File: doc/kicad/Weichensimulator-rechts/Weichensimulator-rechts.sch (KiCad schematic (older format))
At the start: 9 parts, among them J1 Conn_01x02_Male, J2 Power, J3 Conn_01x02_Male, K1 HFD2_005-S-L2-D

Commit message: v2.0 hinzugefügt
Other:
- moved on the sheet: H1
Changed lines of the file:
@@
 Wire Wire Line
 	5450 3250 5450 3150
-Connection ~ 4200 3850
 Wire Wire Line
 	4200 3850 4800 3850
-Connection ~ 4300 3950
 Wire Wire Line
 	4300 3950 4800 3950
-Connection ~ 5450 3150
 Wire Wire Line
 	4350 2300 4500 2300
@@
 L Mechanical:MountingHole H1
 U 1 1 6074DA08
-P 6350 2100
-F 0 "H1" H 6450 2200 50  0000 L CNN
-F 1 "MountingHole" H 6450 2055 50  0001 L CNN
-F 2 "Mounting_Holes:MountingHole_3.2mm_M3" H 6350 2100 50  0001 C CNN
-F 3 "~" H 6350 2100 50  0001 C CNN
-	1    6350 2100
+P 6450 1950
+F 0 "H1" H 6550 2050 50  0000 L CNN
+F 1 "MountingHole" H 6550 1905 50  0001 L CNN
+F 2 "Mounting_Holes:MountingHole_3.2mm_M3" H 6450 1950 50  0001 C CNN
+F 3 "~" H 6450 1950 50  0001 C CNN
+	1    6450 1950
 	1    0    0    -1
 $EndComp
@@
 	1    0    0    -1
 $EndComp
+Connection ~ 5450 3150
+Connection ~ 4200 3850
+Connection ~ 4300 3950
 $EndSCHEMATC

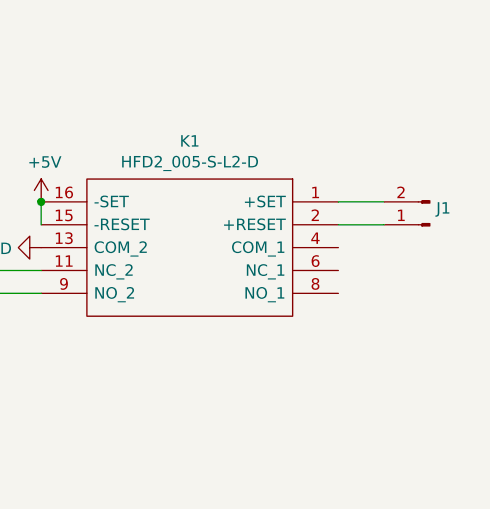
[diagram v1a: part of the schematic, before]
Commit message: 2. Umschalter herausgeführt
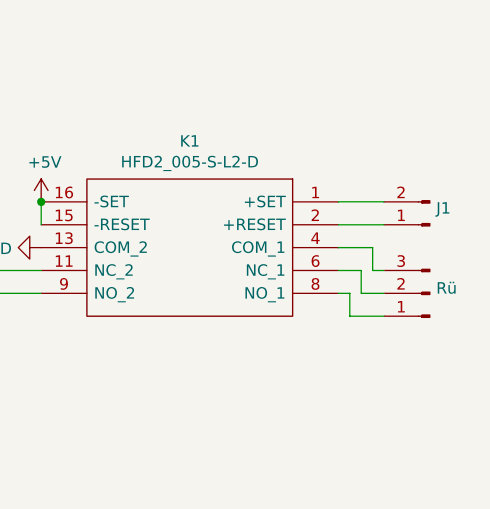
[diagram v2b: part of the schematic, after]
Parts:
- added Rü: Conn_01x03_Male, Pin_Headers:Pin_Header_Straight_1x03_Pitch2.54mm, symbol Connector:Conn_01x03_Male
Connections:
- net at K1.4 (COM_1): now also Rü.3 (Pin_3)
- net at K1.6 (NC_1): now also Rü.2 (Pin_2)
- net at K1.8 (NO_1): now also Rü.1 (Pin_1)
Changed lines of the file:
@@
 Connection ~ 4200 3850
 Connection ~ 4300 3950
+$Comp
+L Connector:Conn_01x03_Male Rü
+U 1 1 60A840A4
+P 7150 3550
+F 0 "Rü" H 7122 3528 50  0000 R CNN
+F 1 "Conn_01x03_Male" H 7122 3573 50  0001 R CNN
+F 2 "Pin_Headers:Pin_Header_Straight_1x03_Pitch2.54mm" H 7150 3550 50  0001 C CNN
+F 3 "~" H 7150 3550 50  0001 C CNN
+	1    7150 3550
+	-1   0    0    1
+$EndComp
+Wire Wire Line
+	6750 3550 6800 3550
+Wire Wire Line
+	6800 3550 6800 3650
+Wire Wire Line
+	6800 3650 6950 3650
+Wire Wire Line
+	6750 3450 6850 3450
+Wire Wire Line
+	6850 3450 6850 3550
+Wire Wire Line
+	6850 3550 6950 3550
+Wire Wire Line
+	6750 3350 6900 3350
+Wire Wire Line
+	6900 3350 6900 3450
+Wire Wire Line
+	6900 3450 6950 3450
 $EndSCHEMATC

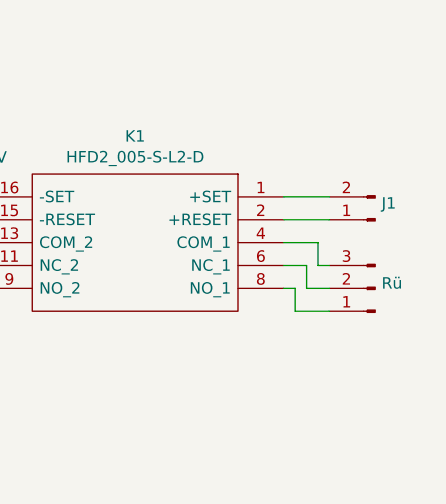
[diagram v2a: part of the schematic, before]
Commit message: Version 2, jetzt korrekt und auch nutzbar für links, 2. Umschalter herausgeführt
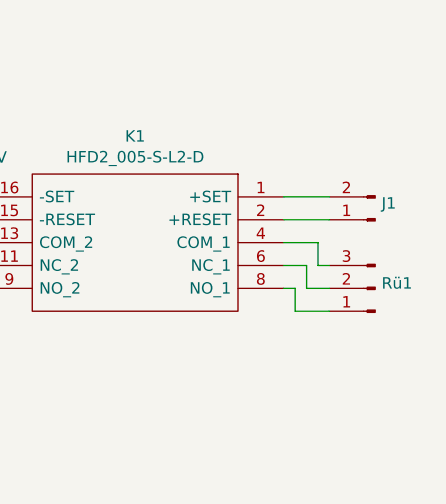
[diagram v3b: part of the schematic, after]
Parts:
- renumbered Rü to Rü1
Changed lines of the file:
@@
 Connection ~ 4300 3950
 $Comp
-L Connector:Conn_01x03_Male Rü
+L Connector:Conn_01x03_Male Rü1
 U 1 1 60A840A4
 P 7150 3550
-F 0 "Rü" H 7122 3528 50  0000 R CNN
+F 0 "Rü1" H 7122 3528 50  0000 R CNN
 F 1 "Conn_01x03_Male" H 7122 3573 50  0001 R CNN
 F 2 "Pin_Headers:Pin_Header_Straight_1x03_Pitch2.54mm" H 7150 3550 50  0001 C CNN

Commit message: Beschriftung für A und G korrigiert, Bauteil-Betruckung auf beiden Seiten
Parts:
- K1: footprint HFD2005SL2D -> HongFa:HFD2005SL2D; symbol HFD2_005-S-L2-D:HFD2_005-S-L2-D -> HongFa:HFD2_005-S-L2-D
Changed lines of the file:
@@
 $EndComp
 $Comp
-L HFD2_005-S-L2-D:HFD2_005-S-L2-D K1
+L HongFa:HFD2_005-S-L2-D K1
 U 1 1 6125B40D
 P 6750 3150
 F 0 "K1" H 7400 3415 50  0000 C CNN
 F 1 "HFD2_005-S-L2-D" H 7400 3324 50  0000 C CNN
-F 2 "HFD2005SL2D" H 7900 3250 50  0001 L CNN
+F 2 "HongFa:HFD2005SL2D" H 7900 3250 50  0001 L CNN
 F 3 "http://www.hongfa.com/pro/pdf/HFD2_en.pdf" H 7900 3150 50  0001 L CNN
 F 4 "Hongfa Europe GMBH DPDT Non-Latching Relay PCB Mount, 5V dc Coil, 3 A, 3 A Subminiature DIP Relay" H 7900 3050 50  0001 L CNN "Description"
